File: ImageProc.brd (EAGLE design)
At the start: 44 x 23.2 mm, 89 parts, among them IC1 XC61GC3002HR-G, IC2 MIC5335-SPYMT, IC5 AT86RF233-ZU, IC6 LTC6088, IC7 DRV8833RTY, IC8 DRV8833RTY, IC9 MPU-6000, J1 CON-HRS-DM3AT, P1 BAT+, P10 MD2, P2 BAT-, P3 MA1, P4 MA2, P5 MB1, P6 MB2, P7 MC1, P8 MC2, P9 MD1, U1 CY8C5688LTI-LP086

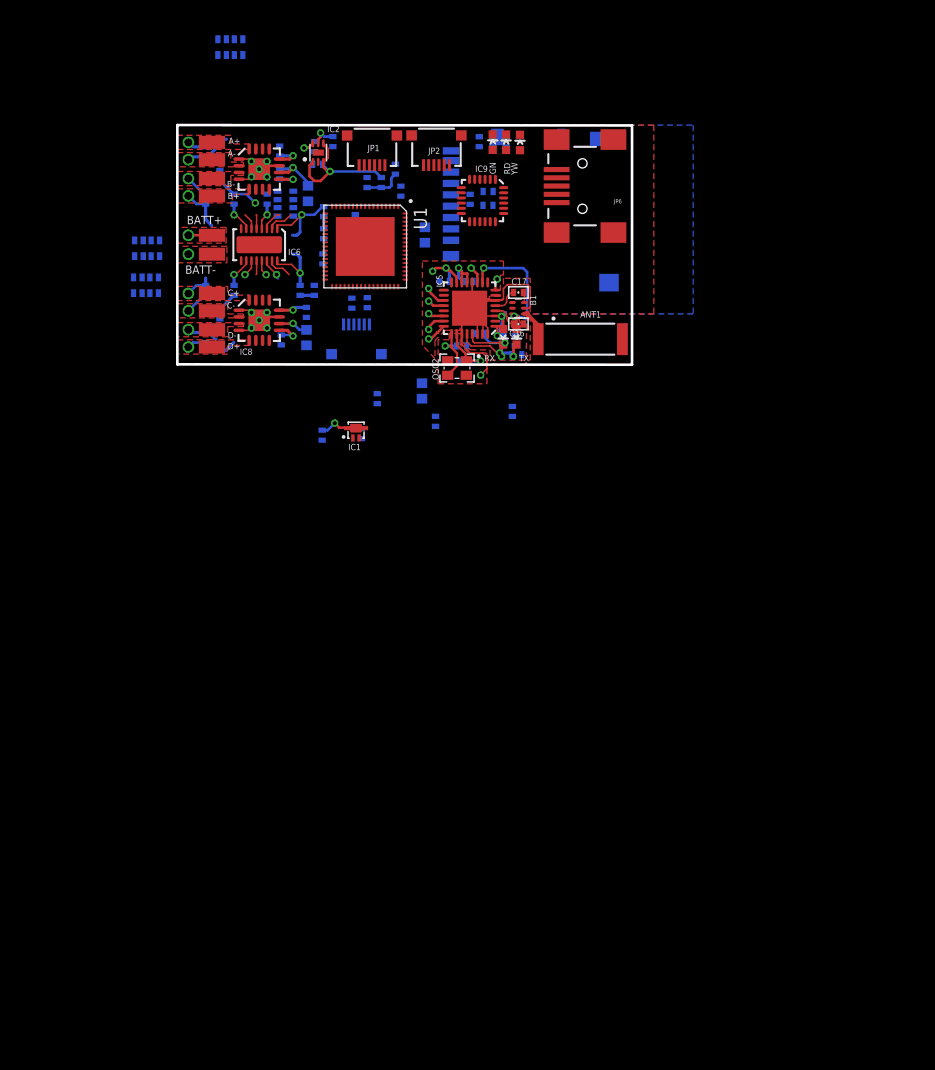
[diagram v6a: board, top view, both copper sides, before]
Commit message: Power routing now in schematic. Prelim boost converter components.
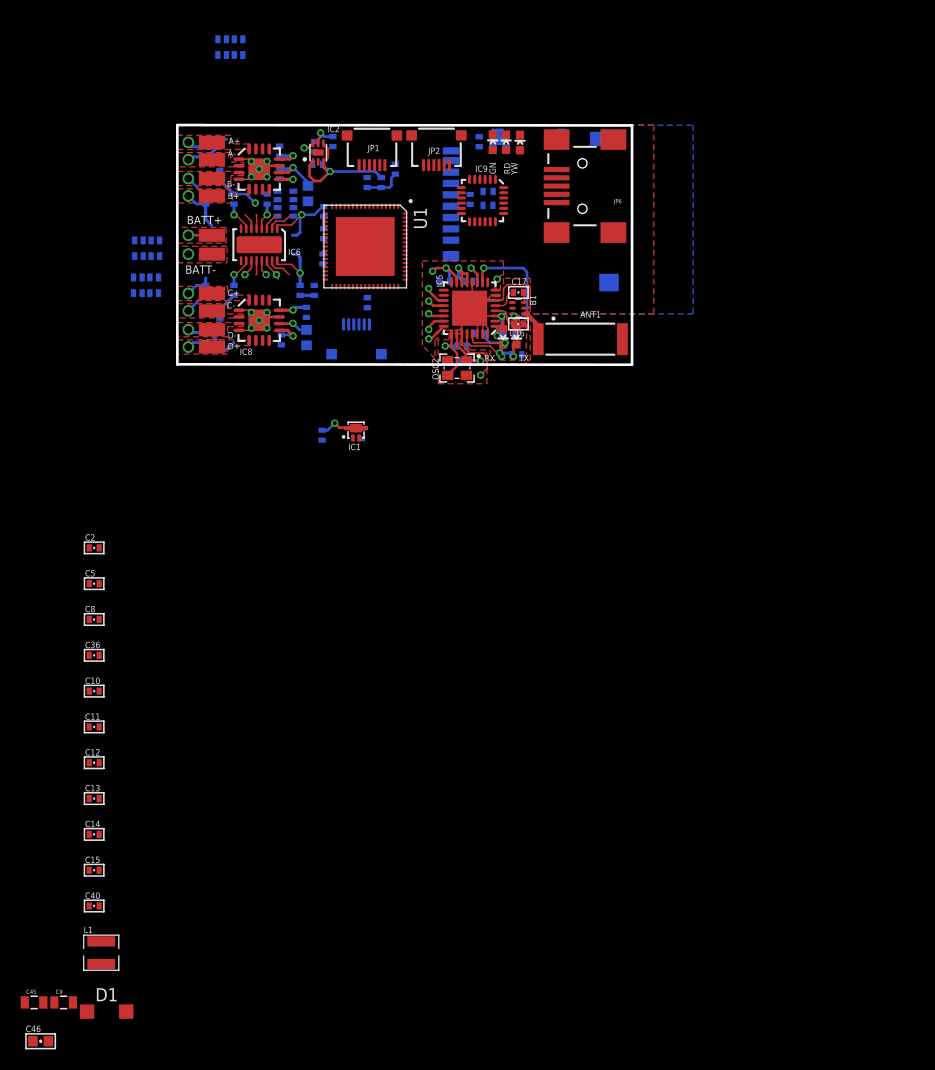
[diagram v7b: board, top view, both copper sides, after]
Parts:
- removed R3: 4.7k, biomimetic:0402-RES
- added C2, C36, C5, C8: 0.1uF, biomimetic:0402-CAP
- added C40: 1.0uF, biomimetic:0402-CAP
- added C45: 22uF, biomimetic:0805
- added C46: .1uF, biomimetic:0603-CAP
- added D1: (no value), diode:SOD123
- C12, C13, C14: value 0.1uF -> 1.0uF
- C15: value 4.7uF -> 0.1uF; device biomimetic:0603-CAP -> biomimetic:0402-CAP
- C9: value 0.1uF -> 22uF; device biomimetic:0402-CAP -> biomimetic:0805
- L1: value 4.7uH -> 10uH; device biomimetic:0603 -> pullin:INDUCTOR_SMD_3X3
- moved L1 76.2 mm to (-7.37, -57.0), flipped to the top, turned to 0 degrees
- moved C9 66.8 mm to (-11.0, -61.8), flipped to the top, turned to 0 degrees
- moved C11 59.8 mm to (-8.05, -35.1), flipped to the top, turned to 0 degrees
- moved C14 57.6 mm to (-8.05, -45.5), flipped to the top, turned to 0 degrees
- moved C15 56.2 mm to (-8.05, -49.0), flipped to the top, turned to 0 degrees
- moved C12 54.8 mm to (-8.05, -38.6), flipped to the top, turned to 0 degrees
- moved C10 52.2 mm to (-8.05, -31.6), flipped to the top, turned to 0 degrees
- moved C13 47.4 mm to (-8.05, -42.0), flipped to the top, turned to 0 degrees
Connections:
- removed net N$28: C15.1
- new net 24MHZ: U1.60
- new net IND: D1.A, L1.P$2, U1.6
- new net VBAT: C9.1, L1.P$1, U1.8
- new net VBOOST: U1.7
- new net VCCA: C14.1, U1.42
- new net VCCD: C40.1, U1.26, U1.57
- new net VDDA: C11.1, C13.1, U1.44
- new net VDDD: C10.1, C12.1, C15.1, C2.1, C36.1, C45.1, C46.1, C5.1, C8.1, D1.C, U1.17, U1.24, U1.35, U1.52, U1.59, U1.67
- new net VSSA: C11.2, C13.2, C14.2, C45.2, C46.2, U1.43
- new net VSSBOOST: C9.2, U1.5
- new net VSSD: C10.2, C12.2, C15.2, C2.2, C36.2, C40.2, C5.2, C8.2, U1.25, U1.45, U1.58, U1.9, U1.CENTER_PAD
- net !XRES: now also U1.10; no longer R3.1
- net 3.3V: no longer C11.1, C12.1, C13.1, C14.1, C9.1, L1.2, R3.2
- net GND: no longer C10.2, C11.2, C12.2, C13.2, C14.2, C15.2, C9.2
- net MOTOR_A_OUT1: now also R33.1
- net MOTOR_A_OUT2: now also R33.2
- net N$21: now also R4.1, U1.50; no longer C10.1, L1.1
- net RADIO_IRQ: now also U1.21
- net RADIO_SLP_TR: now also U1.22
- net SCL1: no longer R4.1, U1.50
- net SWD_SCLK: now also U1.12
- net SWD_SDAT: now also U1.13
- net U2RX: now also U1.53
- net U2TX: now also U1.54
- net V_REF: now also R35.8

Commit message: Proof of concept: signal routing for radio, gyro, and debug port into PSOC arbitrary pins.
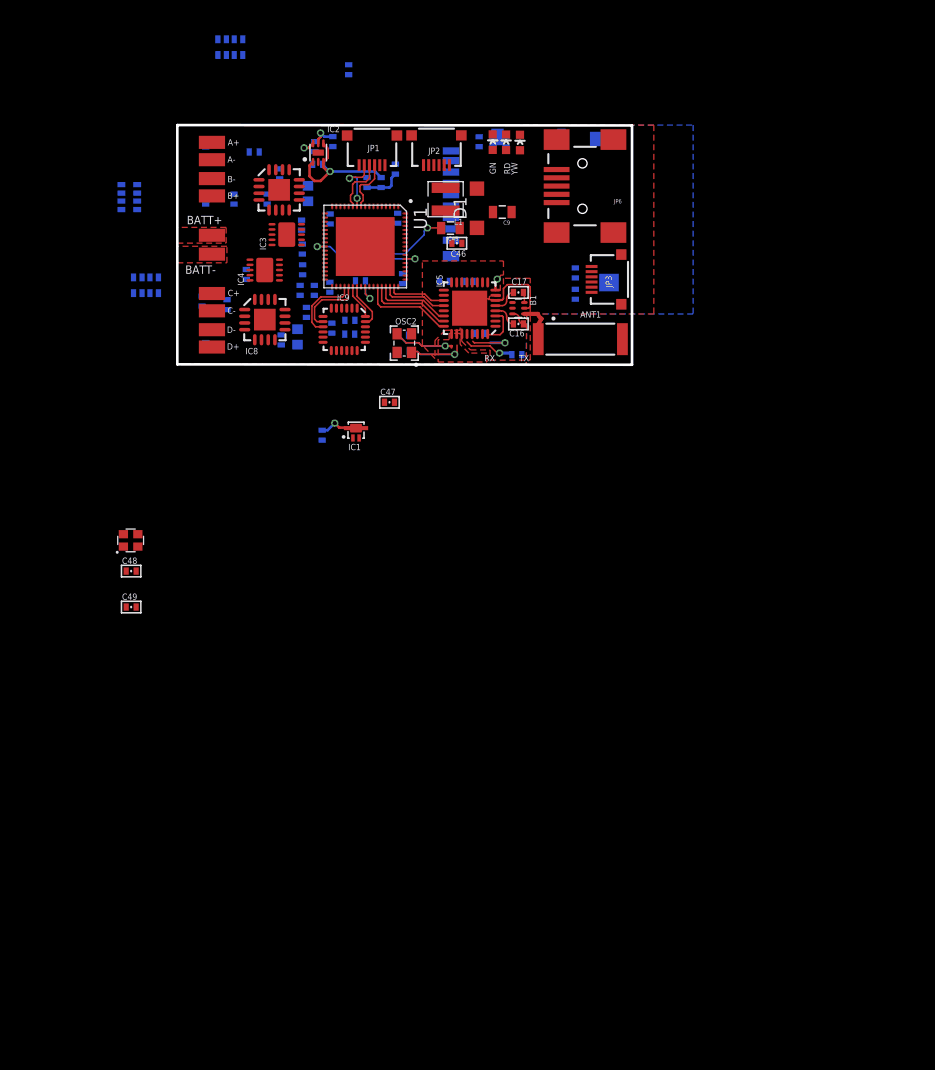
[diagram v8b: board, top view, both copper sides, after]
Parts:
- removed IC6: LTC6088, biomimetic:DFN-16
- removed LED_RX: GREEN, biomimetic:LED-0603
- removed LED_TX: RED, biomimetic:LED-0603
- removed R35: 15k, OPL Eagle Library:R1206-8
- removed R6, R7: 2.7k, biomimetic:0402-RES
- added C47: 0.1uF, biomimetic:0402-CAP
- added C48, C49: 15pF, biomimetic:0402-CAP
- added IC3, IC4: LTC6087, biomimetic:DFN-10
- added U2: SIT8008AI-72-33E-24.000000G, pullin:4-SMD
- C46: value .1uF -> 0.1uF; device biomimetic:0603-CAP -> biomimetic:0402-CAP
- moved C9 87.5 mm to (31.5, 14.7), turned to 180 degrees
- moved C46 87.1 mm to (27.1, 11.7), turned to 180 degrees
- moved D1 85.6 mm to (29.0, 15.1), turned to 90 degrees
- moved C45 85.1 mm to (26.4, 13.2), turned to 180 degrees
- moved L1 80.2 mm to (26.0, 16.0), turned to 180 degrees
- moved C40 71.6 mm to (19.6, 13.7), flipped to the bottom, turned to 180 degrees
- moved C15 67.4 mm to (17.2, 13.6), flipped to the bottom
- moved C14 59.5 mm to (17.7, 8.09), flipped to the bottom, turned to 180 degrees
- moved C13 59.2 mm to (19.8, 10.2), flipped to the bottom, turned to 90 degrees
- moved C12 56.1 mm to (17.3, 11.5), flipped to the bottom
- moved C10 51.7 mm to (19.6, 12.0), flipped to the bottom
- moved C11 51.5 mm to (17.7, 9.45), flipped to the bottom
- moved C36 47.1 mm to (21.8, 8.29), flipped to the bottom, turned to 90 degrees
- moved C5 46.0 mm to (21.3, 14.1), flipped to the bottom, turned to 270 degrees
- moved C8 45.0 mm to (14.8, 14.1), flipped to the bottom, turned to 90 degrees
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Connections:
- removed net N$11: LED_RX.C, R7.1
- removed net N$5: LED_TX.C, R6.1
- new net N$33: JP6.VBUS
- net !SS1: now also U1.47; no longer U1.37
- net 24MHZ: now also C48.1
- net 3.3V: now also C47.1, C49.1, IC3.10, IC4.10, U2.1, U2.4; no longer IC6.4
- net BATT_LEVEL: now also U1.22; no longer U1.11
- net EMFILE_CS: now also J1.2
- net EMFILE_MISO: now also J1.7
- net EMFILE_MOSI: now also J1.3
- net EMFILE_SCK: now also J1.5
- net GND: now also C47.2, C48.2, C49.2, IC3.4, IC3.PAD, IC4.4, IC4.PAD, JP6.GND, U1.25, U1.45, U1.58, U1.9, U2.2; no longer IC6.13, IC6.PAD, R6.2, R7.2
- net MOTOR_B_OUT1: now also R33.3
- net MOTOR_B_OUT2: now also R33.4
- net MOTOR_C_OUT1: now also R34.1
- net MOTOR_C_OUT2: now also R34.2
- net MOTOR_D_OUT1: now also R34.3
- net MOTOR_D_OUT2: now also R34.4
- net N$13: no longer LED_RX.A
- net N$14: no longer LED_TX.A
- net N$21: now also U1.37; no longer U1.50
- net N$22: now also IC3.7; no longer IC6.6
- net N$23: now also IC3.8, R8.5; no longer IC6.5, R35.2
- net N$24: now also IC4.3; no longer IC6.11, R8.3
- net N$25: now also IC4.2; no longer IC6.12, R35.3
- net N$26: now also IC4.7; no longer IC6.15, R8.4
- net N$27: now also IC4.8; no longer IC6.14, R35.4
- net N$30: now also IC3.3; no longer IC6.2
- net N$31: now also IC3.2, R8.6; no longer IC6.3, R35.1
- net N$34: now also IC4.9; no longer IC6.16, R8.5
- net N$35: now also IC4.1; no longer IC6.10, R8.6
- net N$36: now also IC3.1; no longer IC6.1
- net N$37: now also IC3.9; no longer IC6.7
- net RADIO_IRQ: now also U1.46; no longer U1.21
- net RADIO_SLP_TR: now also U1.51; no longer U1.22
- net SCK1: now also U1.50; no longer U1.48
- net SCK2: now also U1.41; no longer U1.49
- net SDA1: now also U1.21; no longer U1.51
- net SDI1: now also U1.49; no longer U1.40
- net SDI2: now also U1.38; no longer U1.41
- net SDO1: now also U1.48; no longer U1.46
- net SDO2: now also U1.40; no longer U1.47
- net SWD_SDAT: now also U1.11; no longer U1.13
- net VSSD: no longer U1.25, U1.45, U1.58, U1.9
- net V_REF: now also R8.3, R8.4; no longer R35.8
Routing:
- net GND: track 42.3 -> 11.1 mm, vias 13 -> 0
- net N$14: track 13.2 -> 0.00 mm, vias 2 -> 0
- net VCCD: track 0.00 -> 11.6 mm, vias 0 -> 2
- net V_BATT: track 28.1 -> 17.8 mm, vias 5 -> 2
- net VSSA: track 0.00 -> 10.2 mm, vias 0 -> 2
- net N$36: track 8.21 -> 0.00 mm, vias 1 -> 0
- net 3.3V: track 15.5 -> 7.39 mm, vias 5 -> 2
- net SDI2: track 0.00 -> 7.24 mm
- net RADIO_IRQ: track 1.97 -> 8.93 mm, vias 1 -> 0
- net !SS2: track 0.00 -> 6.81 mm
- net N$34: track 6.50 -> 0.00 mm, vias 1 -> 0
- net !SS1: track 1.93 -> 8.16 mm, vias 1 -> 0
- net SWD_SDAT: track 0.00 -> 6.02 mm, vias 0 -> 2
- net SDO1: track 1.55 -> 7.41 mm, vias 1 -> 0
- net SWD_SCLK: track 0.00 -> 5.44 mm
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- removed copper zone on layer 1, net MOTOR_A_OUT1
- removed copper zone on layer 1, net MOTOR_A_OUT2
- removed copper zone on layer 1, net MOTOR_B_OUT1
- removed copper zone on layer 1, net MOTOR_B_OUT2
- removed copper zone on layer 1, net MOTOR_C_OUT1
- removed copper zone on layer 1, net MOTOR_C_OUT2
- removed copper zone on layer 1, net MOTOR_D_OUT1
- removed copper zone on layer 1, net MOTOR_D_OUT2
